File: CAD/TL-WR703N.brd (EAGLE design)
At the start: 47.4 x 50 mm, 241 parts, among them T1 H1601CG, U1 AR9331-AL1A, U2 A3S56F40FTP

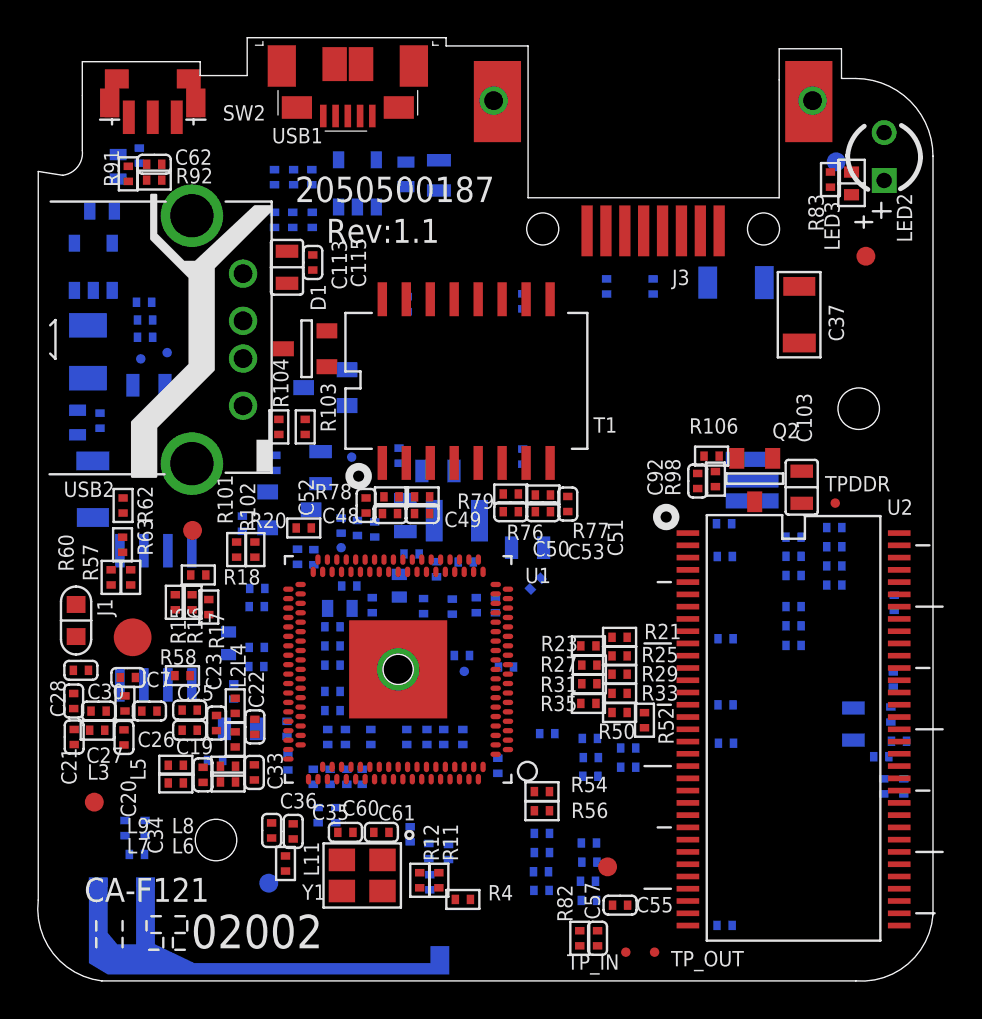
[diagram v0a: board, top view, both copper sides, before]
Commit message: Routed SDRAM
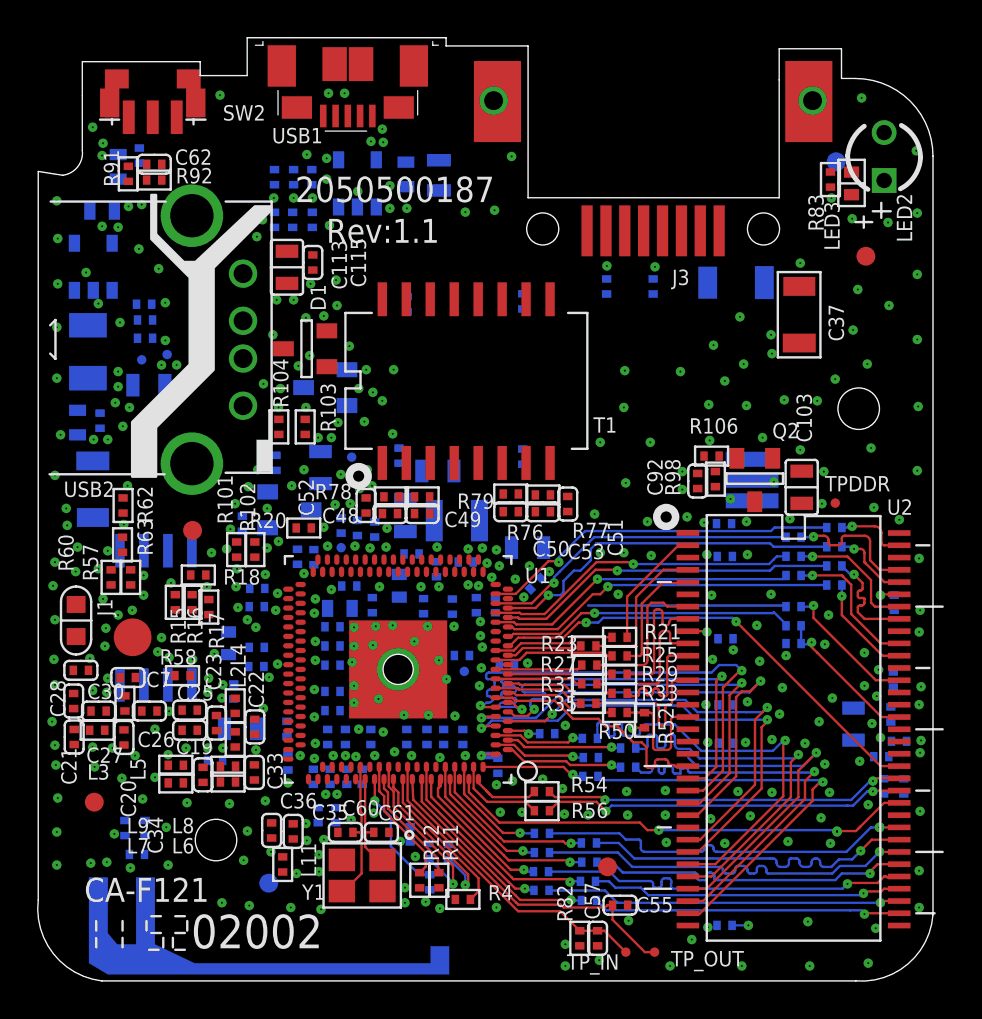
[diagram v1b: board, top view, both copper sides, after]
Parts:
- moved L11 0.16 mm to (13.8, 6.68)
- moved C65 0.11 mm to (25.7, 17.2)
- moved R100 0.10 mm to (6.48, 36.4)
- moved R53 0.10 mm to (40.9, 18.4)
- moved TPGND 0.10 mm to (7.70, 33.7)
- moved TP3V3 0.07 mm to (6.35, 33.4)
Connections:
- removed net VSS: U2.34, U2.48, U2.66
- removed net VSSQ: U2.12, U2.52, U2.58, U2.6, U2.64
- new net GND: C10.1, C66.1, C72.1, R52.2, U2.12, U2.34, U2.48, U2.52, U2.58, U2.6, U2.64, U2.66
- new net S$1: R28.2, U2.32
- new net S$10: R30.2, U2.35
- new net S$11: R32.2, U2.36
- new net S$12: R38.2, U2.39
- new net S$13: R40.2, U2.40
- new net S$14: R46.2, U2.42
- new net S$15: C57.2, R82.2, TP_IN.1, U1.B68
- new net S$16: R21.1, U2.2
- new net S$19: U1.A85, U2.44
- new net S$2: R26.2, U2.31
- new net S$20: R26.1, U1.A3
- new net S$21: R22.1, U1.A4
- new net S$22: R23.1, U2.4
- new net S$23: R25.1, U2.5
- new net S$24: R27.1, U2.7
- new net S$25: R29.1, U2.8
- new net S$26: R31.1, U2.10
- new net S$27: R33.1, U2.11
- new net S$3: R24.2, U2.30
- new net S$30: R35.1, U2.13
- new net S$31: R50.1, R52.1, U2.16
- new net S$32: R21.2, U1.B12
- new net S$33: R23.2, U1.A13
- new net S$34: R25.2, U1.B11
- new net S$344: U1.A14, U2.47
- new net S$345: R37.2, U2.54
- new net S$346: R41.2, U2.57
- new net S$347: R45.2, U2.60
- new net S$348: R48.2, U2.63
- new net S$349: R49.2, U2.65
- new net S$35: R27.2, U1.B10
- new net S$350: R47.2, U2.62
- new net S$351: R43.2, U2.59
- new net S$352: R39.2, U2.56
- new net S$36: R29.2, U1.A11
- new net S$361: R43.1, U1.A17
- new net S$362: R45.1, U1.B16
- new net S$363: R39.1, U1.A16
- new net S$364: R41.1, U1.B15
- new net S$366: R51.1, U1.A15
- new net S$369: R51.2, R53.2, U2.51
- new net S$37: R31.2, U1.B9
- new net S$375: U1.B6, U2.22
- new net S$376: U1.A8, U2.21
- new net S$377: U1.A7, U2.23
- new net S$378: U1.B5, U2.24
- new net S$38: R33.2, U1.A10
- new net S$382: U1.A6, U2.26
- new net S$383: U1.B4, U2.27
- new net S$39: R35.2, U1.B8
- new net S$4: R22.2, U2.29
- new net S$40: R50.2, U1.A9
- new net S$41: R37.1, U1.B14
- new net S$426: R49.1, U1.B18
- new net S$428: R48.1, U1.B17
- new net S$429: R47.1, U1.A18
- new net S$43: R54.1, U1.A86
- new net S$434: C72.2, U1.A5
- new net S$46: R56.1, U1.B75
- new net S$47: R4.1, U1.A78
- new net S$48: C60.2, U1.B63, Y1.3
- new net S$49: C61.1, U1.A74, Y1.1
- new net S$5: R42.2, U2.28
- new net S$51: R12.2, U1.B65
- new net S$52: R11.2, U1.A76
- new net S$53: R54.2, U2.46
- new net S$56: U1.B7, U2.20
- new net S$57: R28.1, U1.B76
- new net S$58: R24.1, U1.B2
- new net S$59: R42.1, U1.B3
- new net S$6: C55.1, TP_OUT.1, U1.A79
- new net S$60: R56.2, U2.45
- new net S$61: R44.1, U1.B73
- new net S$62: R38.1, U1.B72
- new net S$63: R34.1, U1.A81
- new net S$64: R32.1, U1.B70
- new net S$65: R36.1, U1.A82
- new net S$66: R40.1, U1.A83
- new net S$67: R46.1, U1.B74
- new net S$7: R44.2, U2.41
- new net S$74: R30.1, U1.A80
- new net S$76: R2.2, U1.A77
- new net S$77: R3.2, U1.B66
- new net S$8: R36.2, U2.38
- new net S$83: C66.2, U1.B1
- new net S$9: R34.2, U2.37
- new net S$99: R13.1, U1.A75
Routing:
- net S$383: track 0.00 -> 25.8 mm, vias 0 -> 2
- net S$378: track 0.00 -> 25.7 mm, vias 0 -> 2
- net S$375: track 0.00 -> 25.5 mm, vias 0 -> 2
- net S$19: track 0.00 -> 25.1 mm, vias 0 -> 3
- net S$376: track 0.00 -> 24.8 mm, vias 0 -> 2
- net S$344: track 0.00 -> 24.6 mm, vias 0 -> 2
- net S$377: track 0.00 -> 24.3 mm, vias 0 -> 2
- net S$382: track 0.00 -> 23.7 mm, vias 0 -> 2
- net S$5: track 0.00 -> 23.2 mm, vias 0 -> 1
- net S$1: track 0.00 -> 22.5 mm, vias 0 -> 1
- net S$2: track 0.00 -> 21.3 mm, vias 0 -> 1
- net S$4: track 0.00 -> 20.8 mm, vias 0 -> 1
- net S$13: track 0.00 -> 20.4 mm, vias 0 -> 1
- net S$8: track 0.00 -> 20.0 mm, vias 0 -> 1
- net S$14: track 0.00 -> 20.0 mm, vias 0 -> 2
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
